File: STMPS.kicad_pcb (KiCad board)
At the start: 2 copper layers, 85.9 x 44.7 mm, 118 parts, among them P101 12v IN, P102 12v, P103 USB_OTG, P104 E0_THERM, P105 X_STOP, P106 SWD, P107 BED_THERM, P108 Y_STOP, P109 Z_STOP, P201 MOT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

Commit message: Hopefully fix issue with mask/pour clearance.
Correctly tie VREF+ to VCC.
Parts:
- JP101: footprint Pin_Headers:Pin_Header_Straight_1x02_Pitch2.00mm -> Pin_Headers:Pin_Header_Straight_1x02
- moved JP101 0.36 mm to (145.3, 152.1)
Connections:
- net /BED_FET/PWM_IN renamed /BED_PWM
- net /E0_FET/PWM_IN renamed /E0_PWM
- net /E0_Stepper/DIR renamed /E0_DIR
- net /E0_Stepper/ENABLE renamed /E0_ENABLE
- net /E0_Stepper/STEP renamed /E0_STEP
- net /Fan_FET/PWM_IN renamed /FAN_PWM
- net /X_Stepper/DIR renamed /X_DIR
- net /X_Stepper/ENABLE renamed /X_ENABLE
- net /X_Stepper/STEP renamed /X_STEP
- net /Y_Stepper/DIR renamed /Y_DIR
- net /Y_Stepper/ENABLE renamed /Y_ENABLE
- net /Y_Stepper/STEP renamed /Y_STEP
- net /Z_Stepper/DIR renamed /Z_DIR
- net /Z_Stepper/ENABLE renamed /Z_ENABLE
- net /Z_Stepper/STEP renamed /Z_STEP
- C107 pad 1: Net-(C107-Pad1) -> +3.3v
- C109 pad 1: Net-(C107-Pad1) -> +3.3v
- U103 pad 13: Net-(C107-Pad1) -> +3.3v
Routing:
- net +3.3v: track 186.7 -> 197.1 mm, vias 13 -> 14
- net Net-(C107-Pad1): track 5.02 -> 0.00 mm, vias 1 -> 0
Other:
- rule pad_to_mask_clearance: 0.2 -> 0.1524

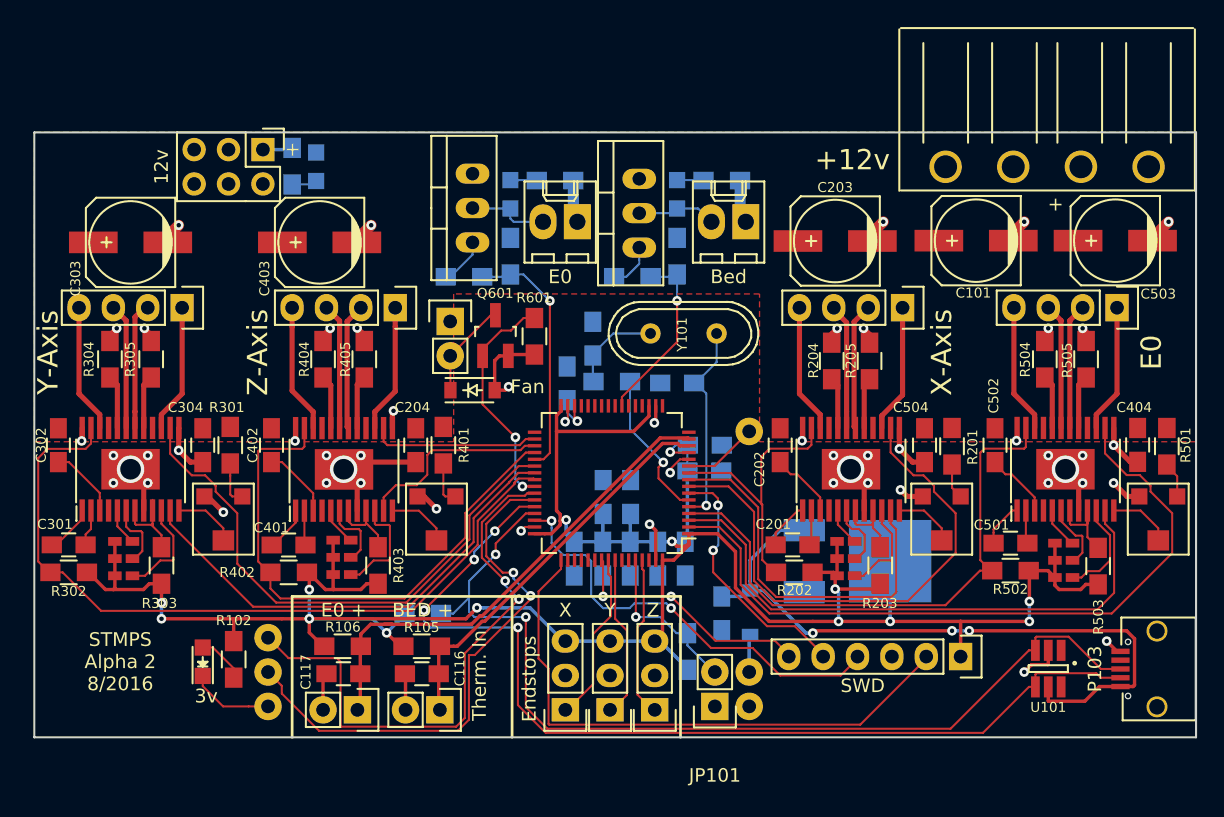
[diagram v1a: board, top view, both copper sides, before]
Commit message: Alpha 3. Fix solder mask clearance. Fix 3.3v not tied to ref+. Tweaks and cleanups.
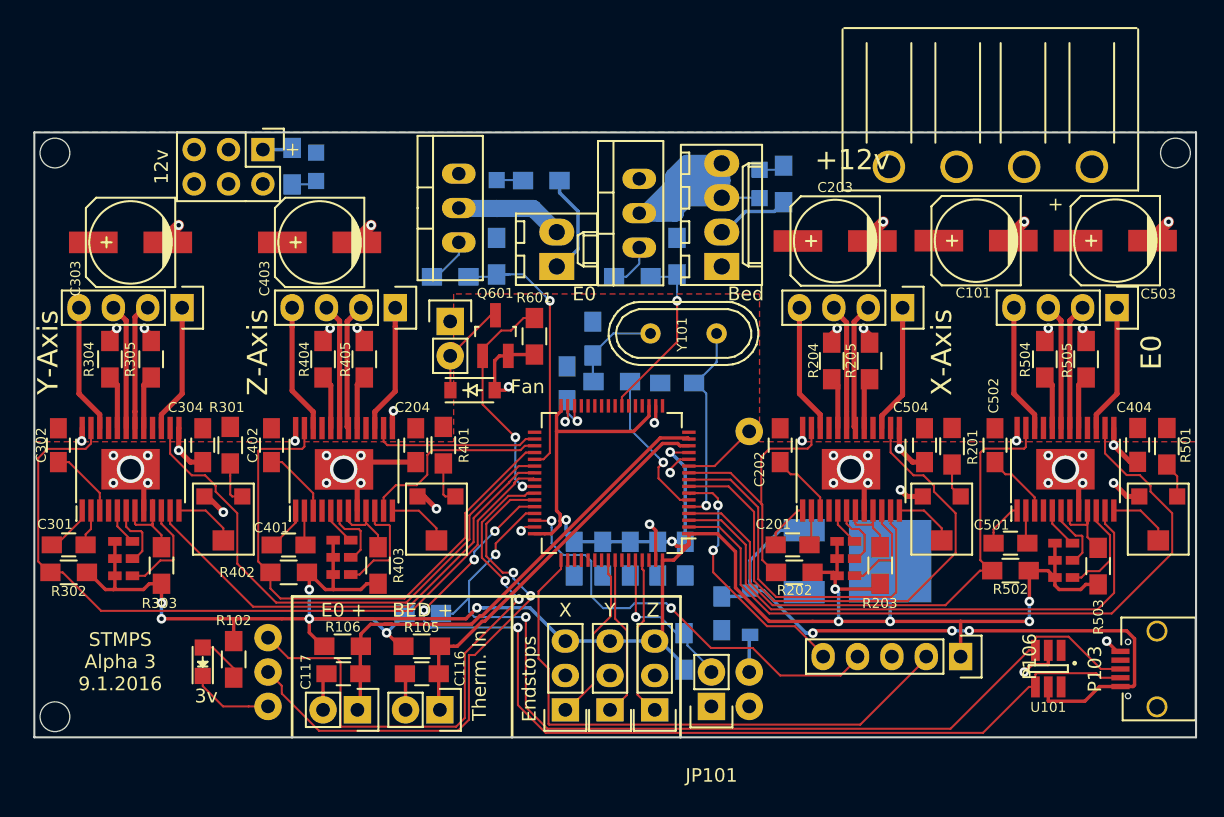
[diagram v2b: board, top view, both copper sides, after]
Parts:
- removed C105, C106, C107: 100nf, Capacitors_SMD:C_0805_HandSoldering
- removed C109: 1uf, Capacitors_SMD:C_0805_HandSoldering
- removed P701, P801: OUT, Connectors_Molex:Molex_KK-6410-02_02x2.54mm_Straight
- added P110: BED, Connectors_Molex:Molex_KK-6410-04_04x2.54mm_Straight, F.Cu at (145.8, 119.6)
- added P111: EO, Connectors_Molex:Molex_KK-6410-02_02x2.54mm_Straight, F.Cu at (133.6, 119.6)
- added REF**: MountingHole_2.2mm_M2, Mounting_Holes:MountingHole_2.2mm_M2, F.Cu at (179.3, 111.3)
- added REF**: MountingHole_2.2mm_M2, Mounting_Holes:MountingHole_2.2mm_M2, F.Cu at (96.5, 152.9)
- added REF**: MountingHole_2.2mm_M2, Mounting_Holes:MountingHole_2.2mm_M2, F.Cu at (96.5, 111.3)
- P106: footprint Pin_Headers:Pin_Header_Straight_1x06 -> Pin_Headers:Pin_Header_Straight_1x05
- moved D801 6.14 mm to (148.6, 113.5)
- moved R803 4.58 mm to (150.4, 113.5), turned to 270 degrees
- moved P101 4.19 mm to (165.6, 112.3)
- moved D701 1.02 mm to (129.2, 114.3)
- moved R701 1.02 mm to (129.2, 118.9)
- moved Q701 1.02 mm to (126.4, 115.3)
- moved R702 1.02 mm to (125.7, 120.4)
- moved R703 1.02 mm to (132.5, 113.3)
- moved JP101 0.25 mm to (145.0, 152.1)
- moved R104 0.25 mm to (143.0, 148.1)
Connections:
- net Net-(D701-Pad1) renamed /E0_FET/OUT-
- net Net-(D801-Pad1) renamed /BED_FET/OUT-
- U103 pad 55: /SWO -> Net-(U103-Pad55)
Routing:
- net /BED_FET/OUT-: track 5.89 -> 26.9 mm
- net /SWO: track 18.4 -> 0.00 mm, vias 2 -> 0
- net +12v: track 8.61 -> 15.7 mm
- net +3.3v: track 197.1 -> 191.2 mm
- net /E0_PWM: track 18.4 -> 20.4 mm
- net /E0_FET/OUT-: track 6.07 -> 7.98 mm
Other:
- rule pad_to_mask_clearance: 0.1524 -> 0.0635
- board text added: "STMPS Alpha 3 9.1.2016"
- board text removed: "STMPS Alpha 2 8/2016"

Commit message: A few more tweaks.
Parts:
- added REF**: MountingHole_2.2mm_M2, Mounting_Holes:MountingHole_2.2mm_M2, F.Cu at (173.7, 152.9)
- added REF**: MountingHole_2.2mm_M2, Mounting_Holes:MountingHole_2.2mm_M2, F.Cu at (179.3, 143.3)
- moved P101 0.47 mm to (166.1, 112.3)
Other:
- board text added: "BOOT"
- board text removed: "+12v"
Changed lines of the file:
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@@
     (links 288)
     (no_connects 0)
-    (area 87.010457 55.271999 188.833543 163.332401)
+    (area 94.920999 109.652999 180.923001 154.507001)
     (thickness 1.6)
-    (drawings 32)
+    (drawings 34)
     (tracks 993)
     (zones 0)
-    (modules 117)
+    (modules 119)
     (nets 136)
   )
@@
   )
   (module Mounting_Holes:MountingHole_2.2mm_M2 (layer F.Cu)
+    (at 173.736 152.908)
+    (descr "Mounting Hole 2.2mm, no annular, M2")
+    (tags "mounting hole 2.2mm no annular m2")
+    (fp_text reference REF** (at 0 -3.2) (layer F.SilkS) hide
+      (effects (font (size 1 1) (thickness 0.15)))
+    )
+    (fp_text value MountingHole_2.2mm_M2 (at 0 3.2) (layer F.Fab)
+      (effects (font (size 1 1) (thickness 0.15)))
+    )
+    (fp_circle (center 0 0) (end 2.2 0) (layer Cmts.User) (width 0.15))
+    (fp_circle (center 0 0) (end 2.45 0) (layer F.CrtYd) (width 0.05))
+    (pad 1 np_thru_hole circle (at 0 0) (size 2.2 2.2) (drill 2.2) (layers *.Cu *.Mask F.SilkS))
+  )
+  (module Mounting_Holes:MountingHole_2.2mm_M2 (layer F.Cu)
+    (at 179.324 143.256)
+    (descr "Mounting Hole 2.2mm, no annular, M2")
+    (tags "mounting hole 2.2mm no annular m2")
+    (fp_text reference REF** (at 0 -3.2) (layer F.SilkS) hide
+      (effects (font (size 1 1) (thickness 0.15)))
+    )
+    (fp_text value MountingHole_2.2mm_M2 (at 0 3.2) (layer F.Fab)
+      (effects (font (size 1 1) (thickness 0.15)))
+    )
+    (fp_circle (center 0 0) (end 2.2 0) (layer Cmts.User) (width 0.15))
+    (fp_circle (center 0 0) (end 2.45 0) (layer F.CrtYd) (width 0.05))
+    (pad 1 np_thru_hole circle (at 0 0) (size 2.2 2.2) (drill 2.2) (layers *.Cu *.Mask F.SilkS))
+  )
+  (module Mounting_Holes:MountingHole_2.2mm_M2 (layer F.Cu)
     (at 179.324 111.252)
     (descr "Mounting Hole 2.2mm, no annular, M2")
@@
     (descr "SMT capacitor, aluminium electrolytic, 6.3x5.8")
     (attr smd)
-    (fp_text reference C101 (at 0.2032 -3.8608 180) (layer F.SilkS)
+    (fp_text reference C101 (at -5.08 -2.159 180) (layer F.SilkS)
       (effects (font (size 0.7366 0.7366) (thickness 0.15)))
     )
@@
     (descr "SMT capacitor, aluminium electrolytic, 6.3x5.8")
     (attr smd)
-    (fp_text reference C203 (at 0 3.9624 360) (layer F.SilkS)
+    (fp_text reference C203 (at -4.826 -2.1336 360) (layer F.SilkS)
       (effects (font (size 0.7366 0.7366) (thickness 0.15)))
     )
@@
     (descr "SMT capacitor, aluminium electrolytic, 6.3x5.8")
     (attr smd)
-    (fp_text reference C503 (at -3.175 -3.937 360) (layer F.SilkS)
+    (fp_text reference C503 (at -3.937 -4.191 360) (layer F.SilkS)
       (effects (font (size 0.7366 0.7366) (thickness 0.15)))
     )
@@
   )
   (module stmps:5EHDRC_1x04 (layer F.Cu)
-    (at 165.648 112.268)
+    (at 166.116 112.268)
     (fp_text reference P101 (at 0 4.318) (layer F.SilkS) hide
       (effects (font (size 0.7366 0.7366) (thickness 0.15)))
@@
     (descr "Through hole pin header")
     (tags "pin header")
-    (fp_text reference JP101 (at 0 -5.1 180) (layer F.SilkS)
+    (fp_text reference JP101 (at 0 -5.1 180) (layer F.SilkS) hide
       (effects (font (size 1 1) (thickness 0.15)))
     )
@@
     (descr "Through hole pin header")
     (tags "pin header")
-    (fp_text reference P106 (at 0 -5.1 270) (layer F.SilkS)
+    (fp_text reference P106 (at 0 -5.1 270) (layer F.SilkS) hide
       (effects (font (size 1 1) (thickness 0.15)))
     )
@@
     (pad 1 np_thru_hole circle (at 0 0) (size 2.2 2.2) (drill 2.2) (layers *.Cu *.Mask F.SilkS))
   )
+  (gr_text "BOOT\n" (at 145.034 147.32) (layer F.SilkS)
+    (effects (font (size 1.016 1.016) (thickness 0.254)))
+  )
+  (gr_text + (at 158.496 114.808 90) (layer F.SilkS)
+    (effects (font (size 1.016 1.016) (thickness 0.254)))
+  )
   (gr_text 12v (at 118.364 112.268) (layer B.SilkS)
     (effects (font (size 1.016 1.016) (thickness 0.254)) (justify mirror))
@@
     (effects (font (size 1.016 1.016) (thickness 0.254)))
   )
-  (gr_text + (at 170.434 115.062 90) (layer F.SilkS)
+  (gr_text + (at 168.656 114.808 90) (layer F.SilkS)
     (effects (font (size 1.016 1.016) (thickness 0.254)))
   )
@@
     (effects (font (size 1.016 1.016) (thickness 0.254)))
   )
-  (gr_text +12v (at 155.448 111.76) (layer F.SilkS)
-    (effects (font (size 1.5 1.5) (thickness 0.3)))
+  (gr_text 12v (at 153.416 112.268) (layer F.SilkS)
+    (effects (font (size 1.27 1.27) (thickness 0.3)))
   )
   (gr_line (start 142.24 57.404) (end 142.494 63.5) (layer Dwgs.User) (width 0.2))
